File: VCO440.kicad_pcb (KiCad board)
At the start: 2 copper layers, 20 x 230.6 mm, 27 parts, among them J1 Conn_01x03, J16 Conn_01x03, J2 Conn_01x03, J3 Conn_01x03, J5 Conn_02x05_Odd_Even, U1 TL074, U3 AS3340

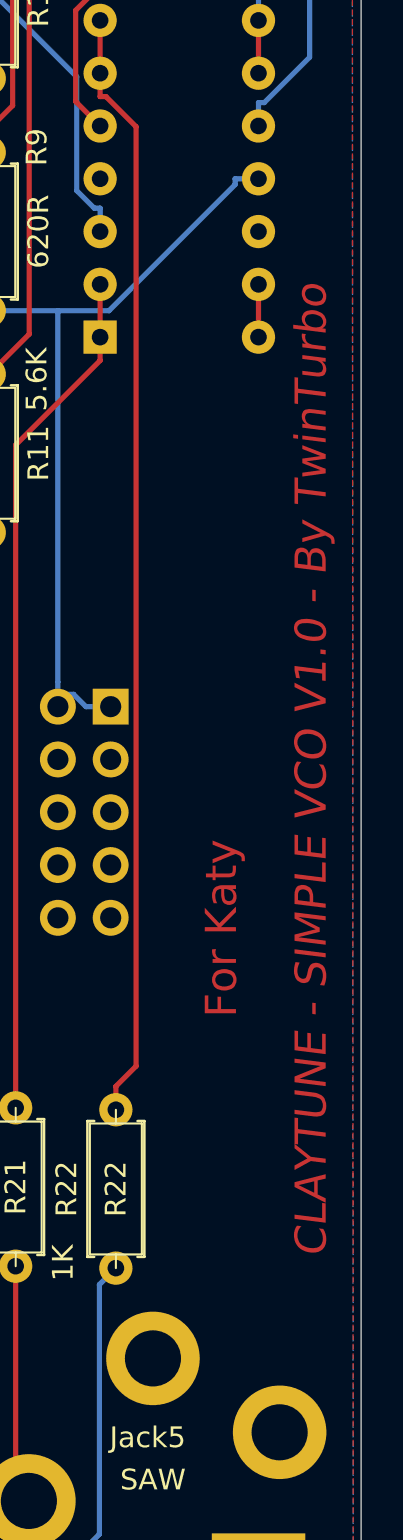
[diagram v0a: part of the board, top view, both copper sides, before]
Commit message: Board Version Number Changed to V0.2 from old Version V1.0
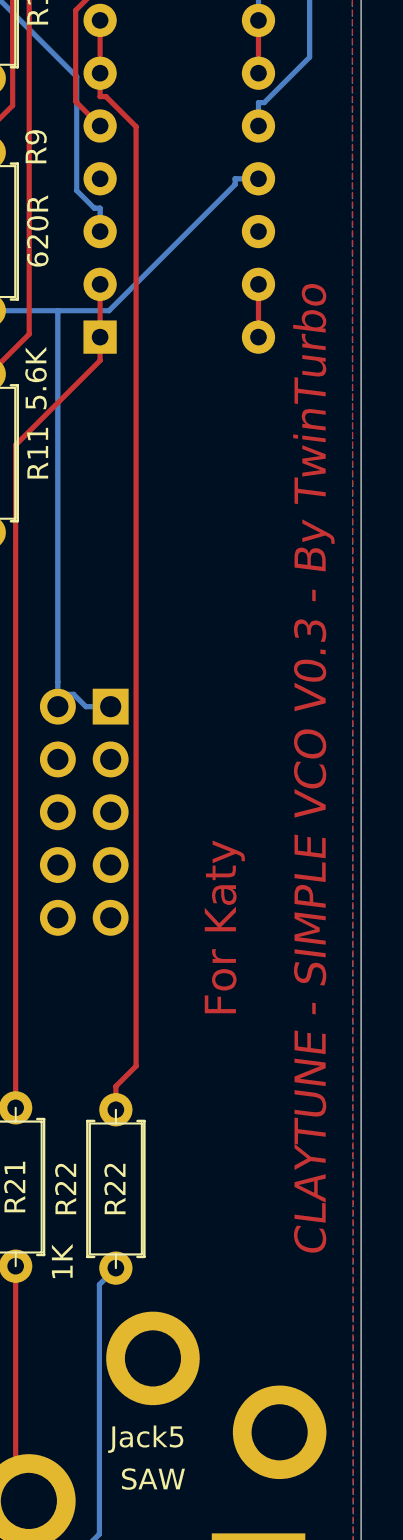
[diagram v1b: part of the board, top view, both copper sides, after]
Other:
- board text added: "CLAYTUNE - SIMPLE VCO V0.3 - By TwinTurbo"
- board text removed: "CLAYTUNE - SIMPLE VCO V1.0 - By TwinTurbo"
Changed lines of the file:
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@@
-(kicad_pcb (version 20171130) (host pcbnew "(5.1.5)-3")
+(kicad_pcb (version 20171130) (host pcbnew 5.1.5-52549c5~86~ubuntu18.04.1)
   (general
     (thickness 1.6)
@@
   (gr_line (start 100 60) (end 100 4.38) (layer Edge.Cuts) (width 0.05))
   (gr_line (start 120 4.38) (end 100 4.38) (layer Edge.Cuts) (width 0.05))
-  (gr_text "CLAYTUNE - SIMPLE VCO V1.0 - By TwinTurbo" (at 117.602 169.672 90) (layer F.Cu)
+  (gr_text "CLAYTUNE - SIMPLE VCO V0.3 - By TwinTurbo" (at 117.602 169.672 90) (layer F.Cu)
     (effects (font (size 1.5 1.5) (thickness 0.3) italic))
   )
